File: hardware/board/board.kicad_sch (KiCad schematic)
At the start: 38 parts, among them J1 DC THRU, J2 DC THRU, J3 DC OUT, J4 DC IN, J5 DC IN, J6 DC OUT, J7 Eurorack Power, J8 Eurorack Power, SW1 ON/OFF, U1 VX7805-500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

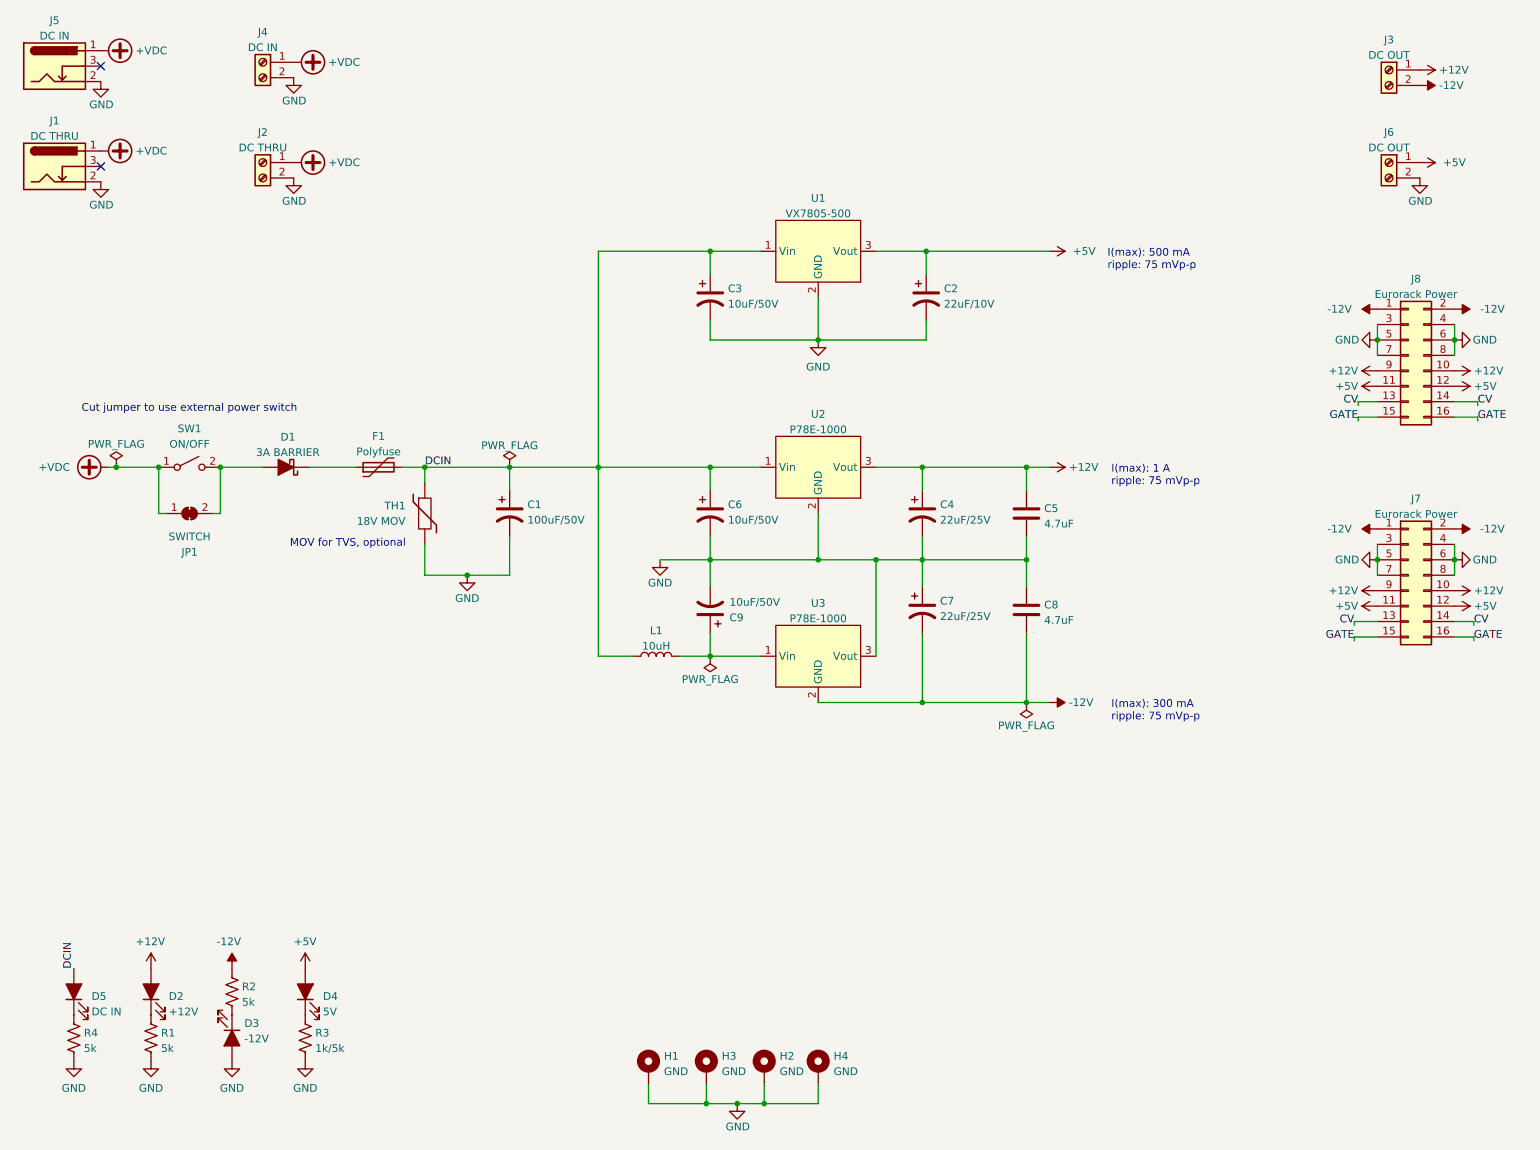
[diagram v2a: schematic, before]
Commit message: Update some MPNs
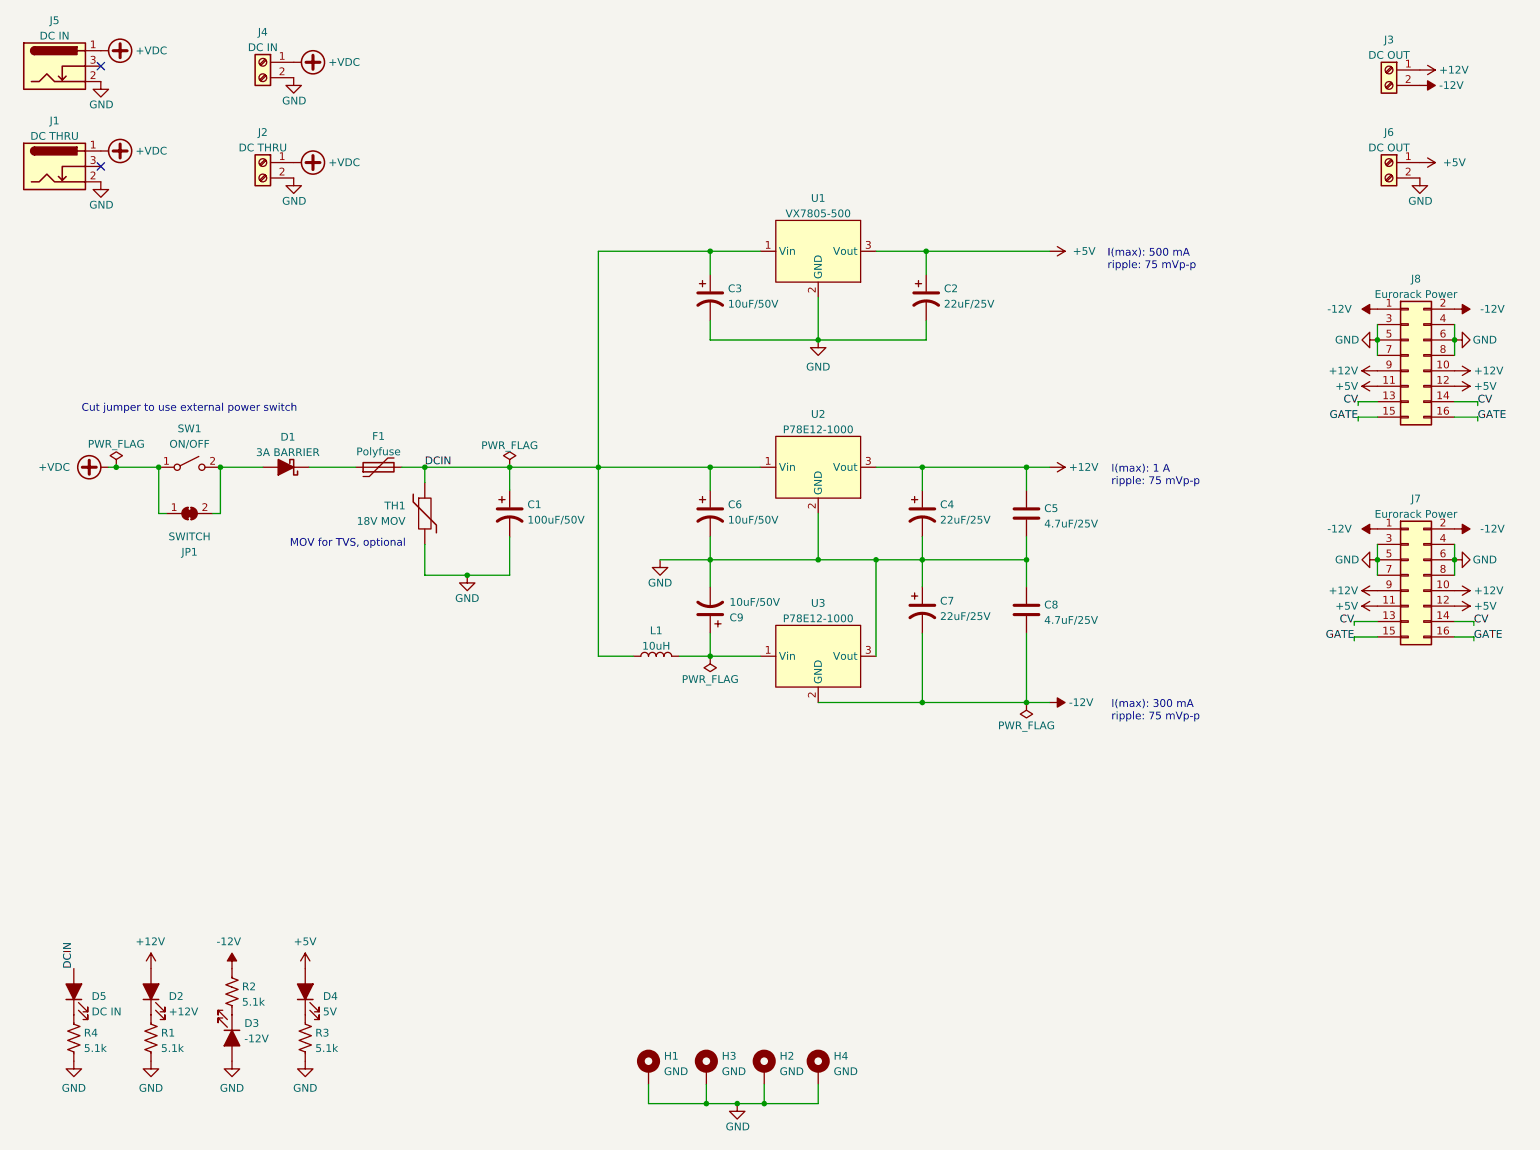
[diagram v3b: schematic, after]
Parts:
- C2: value 22uF/10V -> 22uF/25V
- C5, C8: value 4.7uF -> 4.7uF/25V
- D2, D3, D4, D5: mpn (none) -> APT2012EC
- J3, J6: mpn (none) -> 20020327-C021B01LF
- J7, J8: mpn (none) -> 61201621621
- R1, R2, R4: value 5k -> 5.1k; mpn (none) -> AC0603FR-075K1L
- R3: value 1k/5k -> 5.1k; mpn (none) -> AC0603FR-075K1L
- U1: mpn (none) -> VX7805-500
- U2, U3: value P78E-1000 -> P78E12-1000; mpn (none) -> P78E12-1000
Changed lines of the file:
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@@
       (effects (font (size 1.27 1.27)) (justify left))
     )
-    (property "Value" "4.7uF" (id 1) (at 185.166 115.3672 0)
+    (property "Value" "4.7uF/25V" (id 1) (at 185.166 115.3672 0)
       (effects (font (size 1.27 1.27)) (justify left))
     )
@@
       (effects (font (size 1.27 1.27)) hide)
     )
+    (property "mpn" "APT2012EC" (id 4) (at 51.435 184.15 0)
+      (effects (font (size 1.27 1.27)) hide)
+    )
     (pin "1")
     (pin "2")
@@
     )
     (property "Datasheet" "~" (id 3) (at 63.5 176.53 0)
+      (effects (font (size 1.27 1.27)) hide)
+    )
+    (property "mpn" "APT2012EC" (id 4) (at 63.5 176.53 0)
       (effects (font (size 1.27 1.27)) hide)
     )
@@
       (effects (font (size 1.27 1.27)) hide)
     )
+    (property "mpn" "VX7805-500" (id 4) (at 147.955 54.61 0)
+      (effects (font (size 1.27 1.27)) hide)
+    )
     (pin "1")
     (pin "2")
@@
       (effects (font (size 1.27 1.27)) (justify left))
     )
-    (property "Value" "5k" (id 1) (at 27.051 185.8522 0)
+    (property "Value" "5.1k" (id 1) (at 27.051 185.8522 0)
       (effects (font (size 1.27 1.27)) (justify left))
     )
@@
       (effects (font (size 1.27 1.27)) hide)
     )
+    (property "mpn" "AC0603FR-075K1L" (id 4) (at 25.4 184.15 0)
+      (effects (font (size 1.27 1.27)) hide)
+    )
     (pin "1")
     (pin "2")
@@
     (in_bom yes) (on_board yes) (fields_autoplaced)
     (property "Reference" "U2" (id 0) (at 147.955 81.441 0))
-    (property "Value" "P78E-1000" (id 1) (at 147.955 83.9779 0))
+    (property "Value" "P78E12-1000" (id 1) (at 147.955 83.9779 0))
     (property "Footprint" "winterbloom:Converter_DCDC_CUI_P78E-1000_THT" (id 2) (at 147.955 90.17 0)
       (effects (font (size 1.27 1.27)) hide)
     )
     (property "Datasheet" "https://www.mouser.com/datasheet/2/670/p78e_1000-1480573.pdf" (id 3) (at 147.955 90.17 0)
+      (effects (font (size 1.27 1.27)) hide)
+    )
+    (property "mpn" "P78E12-1000" (id 4) (at 147.955 90.17 0)
       (effects (font (size 1.27 1.27)) hide)
     )
@@
       (effects (font (size 1.27 1.27)) hide)
     )
+    (property "mpn" " 20020327-C021B01LF" (id 4) (at 241.935 40.005 0)
+      (effects (font (size 1.27 1.27)) hide)
+    )
     (pin "1")
     (pin "2")
@@
       (effects (font (size 1.27 1.27)) hide)
     )
+    (property "mpn" "APT2012EC" (id 4) (at 25.4 176.53 0)
+      (effects (font (size 1.27 1.27)) hide)
+    )
     (pin "1")
     (pin "2")
@@
     )
     (property "Datasheet" "~" (id 3) (at 38.1 176.53 0)
+      (effects (font (size 1.27 1.27)) hide)
+    )
+    (property "mpn" "APT2012EC" (id 4) (at 38.1 176.53 0)
       (effects (font (size 1.27 1.27)) hide)
     )
@@
     )
     (property "Datasheet" "~" (id 3) (at 245.11 71.755 0)
+      (effects (font (size 1.27 1.27)) hide)
+    )
+    (property "mpn" "61201621621" (id 4) (at 245.11 71.755 0)
       (effects (font (size 1.27 1.27)) hide)
     )
@@
       (effects (font (size 1.27 1.27)) (justify left))
     )
-    (property "Value" "4.7uF" (id 1) (at 185.166 99.4922 0)
+    (property "Value" "4.7uF/25V" (id 1) (at 185.166 99.4922 0)
       (effects (font (size 1.27 1.27)) (justify left))
     )
@@
       (effects (font (size 1.27 1.27)) (justify left))
     )
-    (property "Value" "22uF/10V" (id 1) (at 168.656 63.2972 0)
+    (property "Value" "22uF/25V" (id 1) (at 168.656 63.2972 0)
       (effects (font (size 1.27 1.27)) (justify left))
     )
@@
       (effects (font (size 1.27 1.27)) hide)
     )
+    (property "mpn" " 20020327-C021B01LF" (id 4) (at 241.935 24.765 0)
+      (effects (font (size 1.27 1.27)) hide)
+    )
     (pin "1")
     (pin "2")
@@
       (effects (font (size 1.27 1.27)) (justify left))
     )
-    (property "Value" "1k/5k" (id 1) (at 65.151 185.8522 0)
+    (property "Value" "5.1k" (id 1) (at 65.151 185.8522 0)
       (effects (font (size 1.27 1.27)) (justify left))
     )
@@
     )
     (property "Datasheet" "~" (id 3) (at 63.5 184.15 0)
+      (effects (font (size 1.27 1.27)) hide)
+    )
+    (property "mpn" "AC0603FR-075K1L" (id 4) (at 63.5 184.15 0)
       (effects (font (size 1.27 1.27)) hide)
     )
@@
     (in_bom yes) (on_board yes) (fields_autoplaced)
     (property "Reference" "U3" (id 0) (at 147.955 112.556 0))
-    (property "Value" "P78E-1000" (id 1) (at 147.955 115.0929 0))
+    (property "Value" "P78E12-1000" (id 1) (at 147.955 115.0929 0))
     (property "Footprint" "winterbloom:Converter_DCDC_CUI_P78E-1000_THT" (id 2) (at 147.955 121.285 0)
       (effects (font (size 1.27 1.27)) hide)
@@
       (effects (font (size 1.27 1.27)) hide)
     )
+    (property "mpn" "P78E12-1000" (id 4) (at 147.955 121.285 0)
+      (effects (font (size 1.27 1.27)) hide)
+    )
     (pin "1")
     (pin "2")
@@
       (effects (font (size 1.27 1.27)) (justify left))
     )
-    (property "Value" "5k" (id 1) (at 53.086 178.2322 0)
+    (property "Value" "5.1k" (id 1) (at 53.086 178.2322 0)
       (effects (font (size 1.27 1.27)) (justify left))
     )
@@
       (effects (font (size 1.27 1.27)) hide)
     )
+    (property "mpn" "AC0603FR-075K1L" (id 4) (at 51.435 176.53 0)
+      (effects (font (size 1.27 1.27)) hide)
+    )
     (pin "1")
     (pin "2")
@@
       (effects (font (size 1.27 1.27)) (justify left))
     )
-    (property "Value" "5k" (id 1) (at 39.751 185.8522 0)
+    (property "Value" "5.1k" (id 1) (at 39.751 185.8522 0)
       (effects (font (size 1.27 1.27)) (justify left))
     )
@@
     )
     (property "Datasheet" "~" (id 3) (at 38.1 184.15 0)
+      (effects (font (size 1.27 1.27)) hide)
+    )
+    (property "mpn" "AC0603FR-075K1L" (id 4) (at 38.1 184.15 0)
       (effects (font (size 1.27 1.27)) hide)
     )
@@
     )
     (property "Datasheet" "~" (id 3) (at 245.11 107.95 0)
+      (effects (font (size 1.27 1.27)) hide)
+    )
+    (property "mpn" "61201621621" (id 4) (at 245.11 107.95 0)
       (effects (font (size 1.27 1.27)) hide)
     )
@@
     )
     (path "/93ac35cd-ac5f-4a30-8dd4-e53b4cd11333"
-      (reference "C2") (unit 1) (value "22uF/10V") (footprint "Capacitor_SMD:C_0805_2012Metric_Pad1.18x1.45mm_HandSolder")
+      (reference "C2") (unit 1) (value "22uF/25V") (footprint "Capacitor_SMD:C_0805_2012Metric_Pad1.18x1.45mm_HandSolder")
     )
     (path "/5c664b41-3687-4c5b-8474-62626090618f"
@@
     )
     (path "/5fae4d05-80e3-4b2d-af81-f76bc49721d3"
-      (reference "C5") (unit 1) (value "4.7uF") (footprint "Capacitor_SMD:C_0805_2012Metric_Pad1.18x1.45mm_HandSolder")
+      (reference "C5") (unit 1) (value "4.7uF/25V") (footprint "Capacitor_SMD:C_0805_2012Metric_Pad1.18x1.45mm_HandSolder")
     )
     (path "/4a28271b-e21e-485b-968b-c9ecd395359e"
@@
     )
     (path "/000452fe-6dbc-471a-9934-e97eb0a9b3b3"
-      (reference "C8") (unit 1) (value "4.7uF") (footprint "Capacitor_SMD:C_0805_2012Metric_Pad1.18x1.45mm_HandSolder")
+      (reference "C8") (unit 1) (value "4.7uF/25V") (footprint "Capacitor_SMD:C_0805_2012Metric_Pad1.18x1.45mm_HandSolder")
     )
     (path "/76d85faa-e47f-495d-84ff-cc0905aaa30d"
@@
     )
     (path "/d78ba7db-3c6a-43f8-b465-38e57b53e249"
-      (reference "R1") (unit 1) (value "5k") (footprint "Resistor_SMD:R_0603_1608Metric_Pad0.98x0.95mm_HandSolder")
+      (reference "R1") (unit 1) (value "5.1k") (footprint "Resistor_SMD:R_0603_1608Metric_Pad0.98x0.95mm_HandSolder")
     )
     (path "/c8bec220-c9b8-4e07-8ba5-d2a26eae602c"
-      (reference "R2") (unit 1) (value "5k") (footprint "Resistor_SMD:R_0603_1608Metric_Pad0.98x0.95mm_HandSolder")
+      (reference "R2") (unit 1) (value "5.1k") (footprint "Resistor_SMD:R_0603_1608Metric_Pad0.98x0.95mm_HandSolder")
     )
     (path "/b6ee61cd-2551-4d36-aada-3743b5d61803"
-      (reference "R3") (unit 1) (value "1k/5k") (footprint "Resistor_SMD:R_0603_1608Metric_Pad0.98x0.95mm_HandSolder")
+      (reference "R3") (unit 1) (value "5.1k") (footprint "Resistor_SMD:R_0603_1608Metric_Pad0.98x0.95mm_HandSolder")
     )
     (path "/1a37e81e-f670-44e7-9ee7-3e0ac81289a6"
-      (reference "R4") (unit 1) (value "5k") (footprint "Resistor_SMD:R_0603_1608Metric_Pad0.98x0.95mm_HandSolder")
+      (reference "R4") (unit 1) (value "5.1k") (footprint "Resistor_SMD:R_0603_1608Metric_Pad0.98x0.95mm_HandSolder")
     )
     (path "/05cdb9b6-c0dc-4fe6-92b4-e0c4062a70ca"
@@
     )
     (path "/22836a84-b49b-4545-bc98-bc59bbc21932"
-      (reference "U2") (unit 1) (value "P78E-1000") (footprint "winterbloom:Converter_DCDC_CUI_P78E-1000_THT")
+      (reference "U2") (unit 1) (value "P78E12-1000") (footprint "winterbloom:Converter_DCDC_CUI_P78E-1000_THT")
     )
     (path "/c5dbc2f4-347d-4e8b-9dc5-05ae6c8ee4e9"
-      (reference "U3") (unit 1) (value "P78E-1000") (footprint "winterbloom:Converter_DCDC_CUI_P78E-1000_THT")
-    )
-  )
+      (reference "U3") (unit 1) (value "P78E12-1000") (footprint "winterbloom:Converter_DCDC_CUI_P78E-1000_THT")
+    )
+  )

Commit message: Use hatched fills
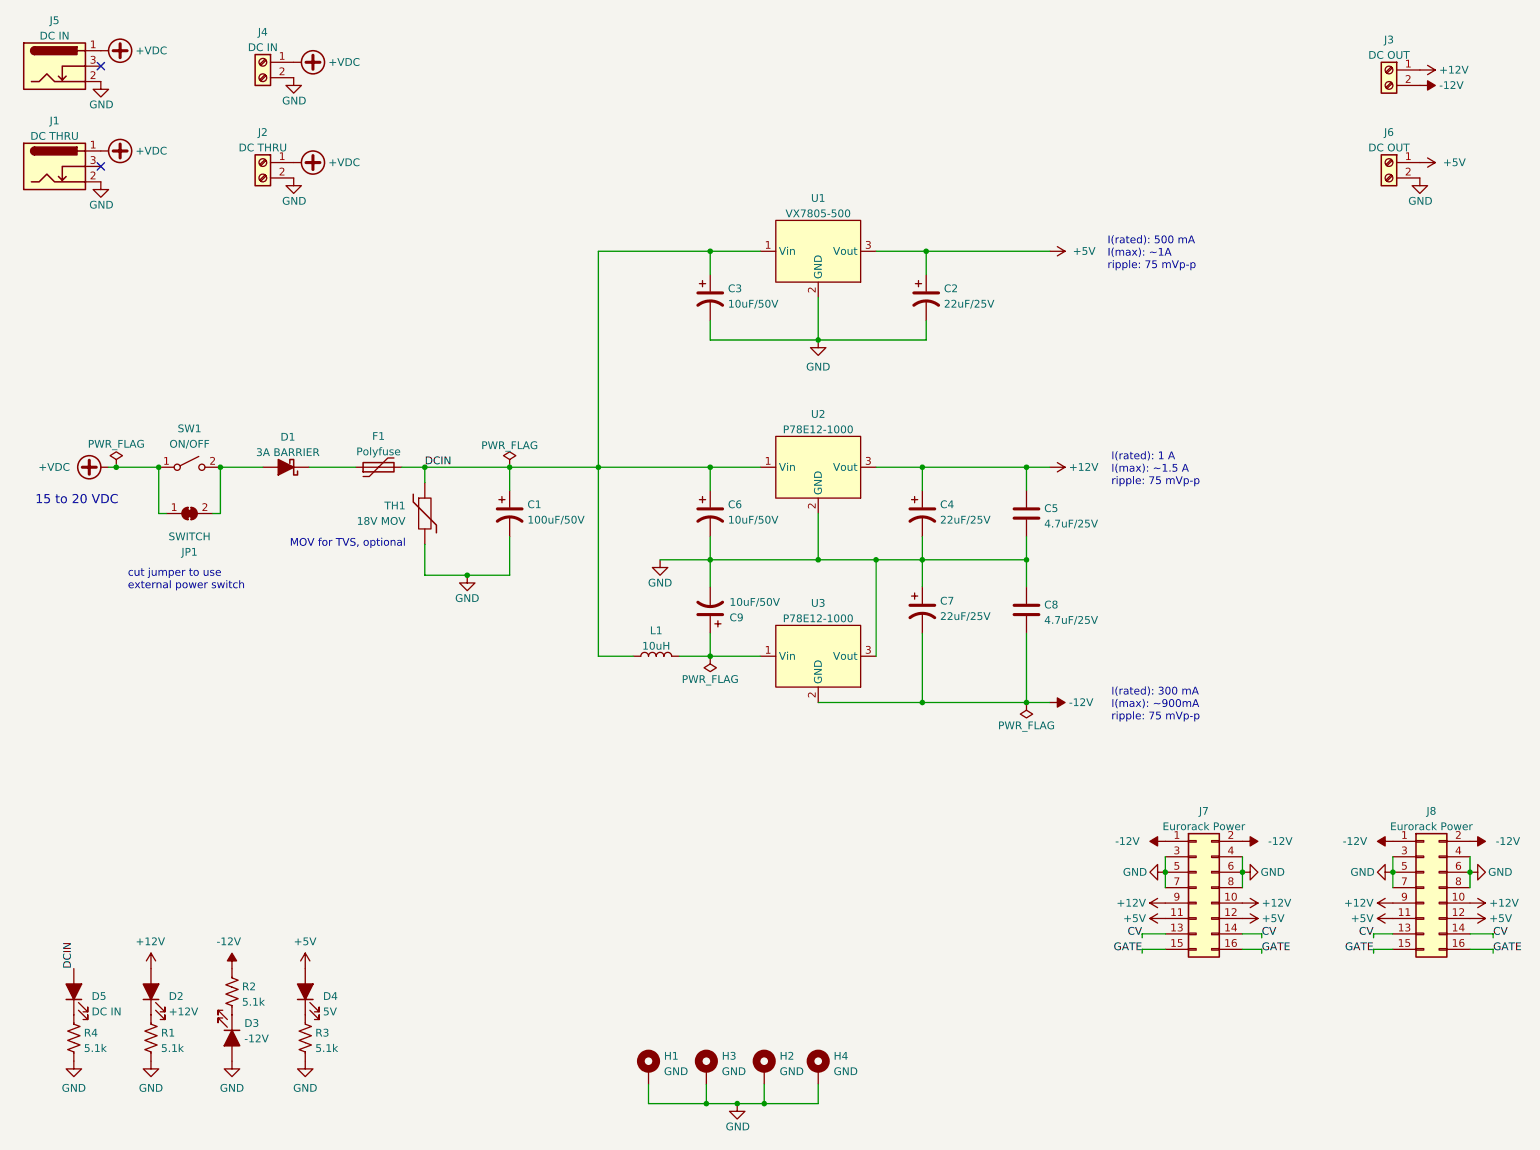
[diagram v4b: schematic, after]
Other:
- note added: "15 to 20 VDC"
- note added: "I(rated): 1 A I(max): ~1.5 A ripple: 75 mVp-p"
- note added: "I(rated): 300 mA I(max): ~900mA ripple: 75 mVp-p"
- note added: "I(rated): 500 mA I(max): ~1A ripple: 75 mVp-p"
- note added: "cut jumper to use external power switch"
- note removed: "Cut jumper to use external power switch"
- note removed: "I(max): 1 A ripple: 75 mVp-p"
- note removed: "I(max): 300 mA ripple: 75 mVp-p"
- note removed: "I(max): 500 mA ripple: 75 mVp-p"
- moved on the sheet: J7, J8
